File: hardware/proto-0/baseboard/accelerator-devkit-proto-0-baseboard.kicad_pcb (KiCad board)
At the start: 6 copper layers, 50 x 42 mm, 175 parts, among them J1 JTAG, J2 USB-C, J3 HDMI, J4 Qwiic I2C, J5 Pmod 1A, J6 Pmod 1B, J7 Display, J8 microSD-ST11-H, Q1 CSD13381F4, SW1 BUTTON1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

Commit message: Onigiri <3
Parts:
- LOGO2: moved to B.Cu
- LOGO3: moved to F.Cu
- moved LOGO2 0.11 mm to (6.55, 26.4), turned to 180 degrees
- moved LOGO3 0.05 mm to (6.60, 26.1), turned to 10 degrees

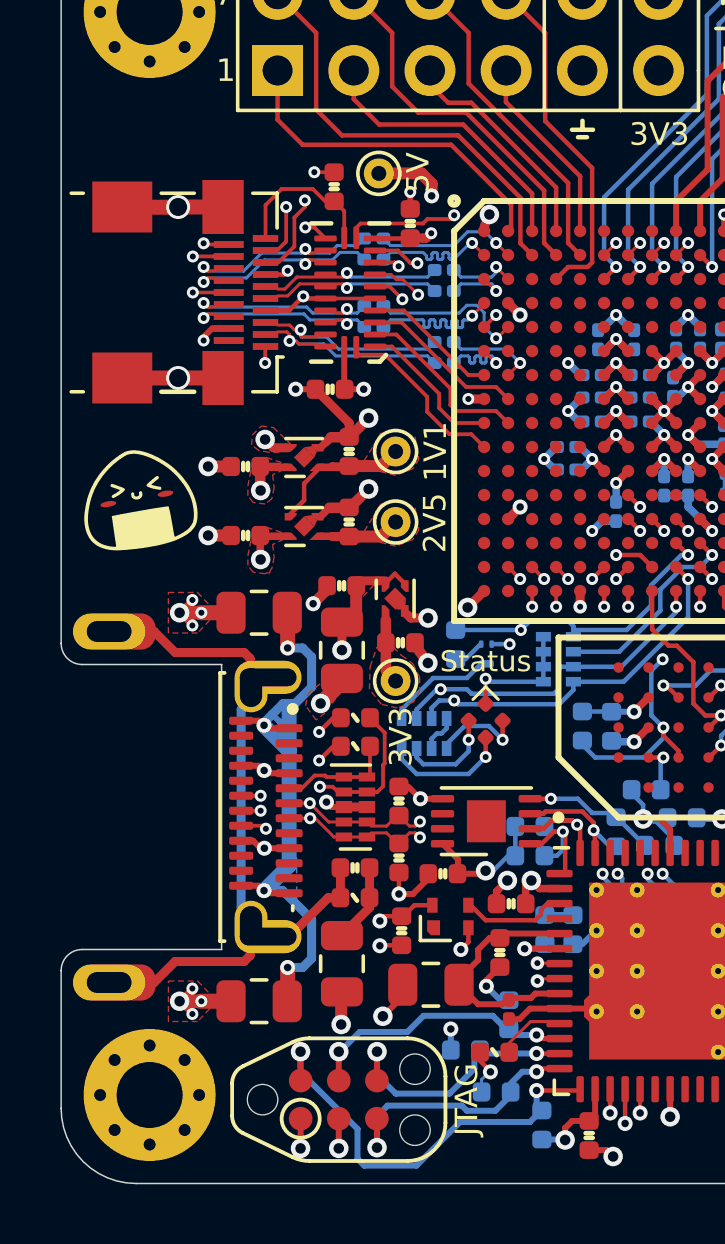
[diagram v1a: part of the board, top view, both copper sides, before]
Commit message: Switching USB connector to CUI UJ31-CH-3-MSMT-TR-67
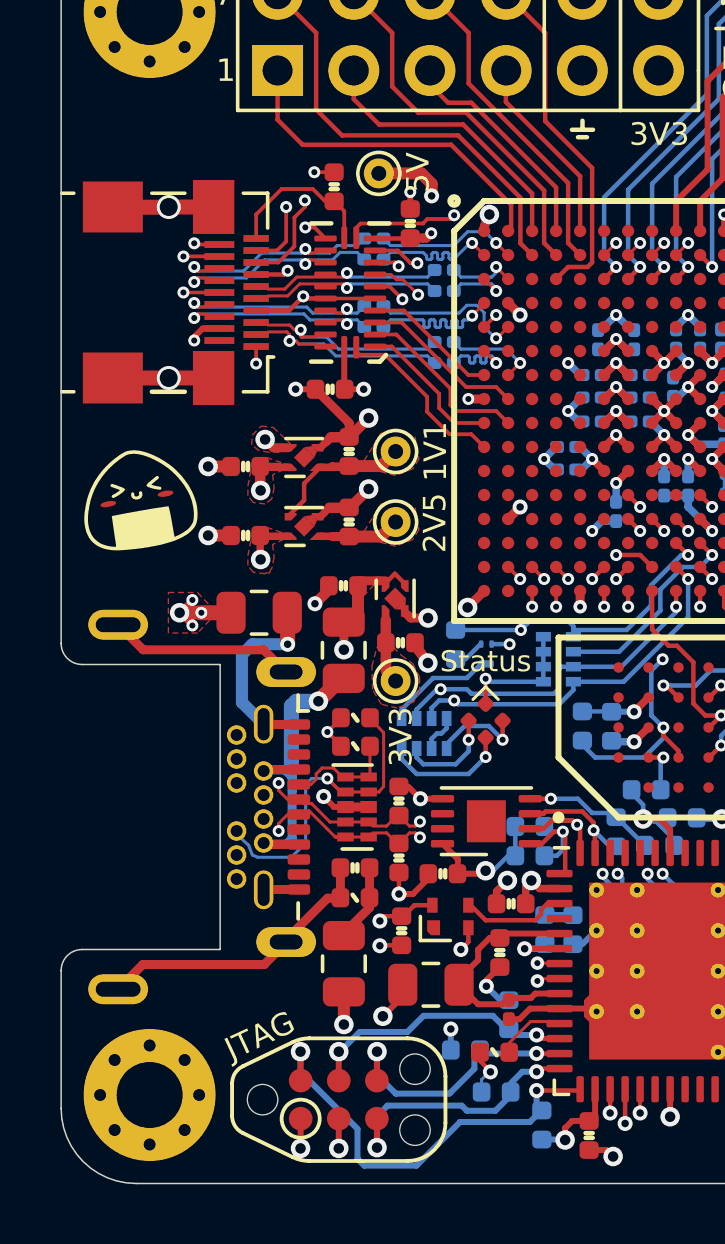
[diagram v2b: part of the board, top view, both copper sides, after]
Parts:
- removed FB5: 1K/1A, Inductor_SMD:L_0805_2012Metric
- J2: footprint Connector_USB_RD:JAE_DX07B024JJ1R1500 -> Connector_USB_RD:CUI_UJ31-CH-3-MSMT-TR-67
- moved J2 5.00 mm to (5.90, 36.5)
- moved J3 0.31 mm to (5.72, 19.3)
- moved FB4 0.07 mm to (13.4, 41.7)
- moved C1 0.06 mm to (13.4, 29.1)
- moved FB1 0.06 mm to (13.4, 31.2)
- moved U9 0.05 mm to (13.9, 36.5)
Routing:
- net /USB-I/O/USB_UNSAFE_GND: track 22.2 -> 13.9 mm, vias 4 -> 1
- net /USB-I/O/USB_SHIELD: track 21.8 -> 25.7 mm
- net GND: track 174.1 -> 170.4 mm, vias 127 -> 122
- net /USB-I/O/USB_CC2: track 9.39 -> 10.7 mm, vias 2 -> 1
- net /USB-I/O/USB_D-: track 17.5 -> 16.4 mm, vias 4 -> 3
- net /USB-I/O/USB_D+: track 17.5 -> 16.7 mm, vias 4 -> 3
- net /HDMI-IO/HDMI_CON_SCL: track 10.1 -> 10.8 mm
- net /HDMI-IO/HDMI_CON_CEC: track 11.5 -> 12.2 mm
- net /HDMI-IO/HDMI_CON_TMDS_CK-: track 6.84 -> 7.46 mm
- net /HDMI-IO/HDMI_CON_TMDS_D1-: track 6.57 -> 7.09 mm
- net /USB-I/O/USB_UNSAFE_VBUS: track 10.5 -> 10.6 mm, vias 3 -> 1
- removed copper zone on B.Cu, net /USB-I/O/USB_UNSAFE_GND
- removed copper zone on F.Cu, net /USB-I/O/USB_UNSAFE_VBUS

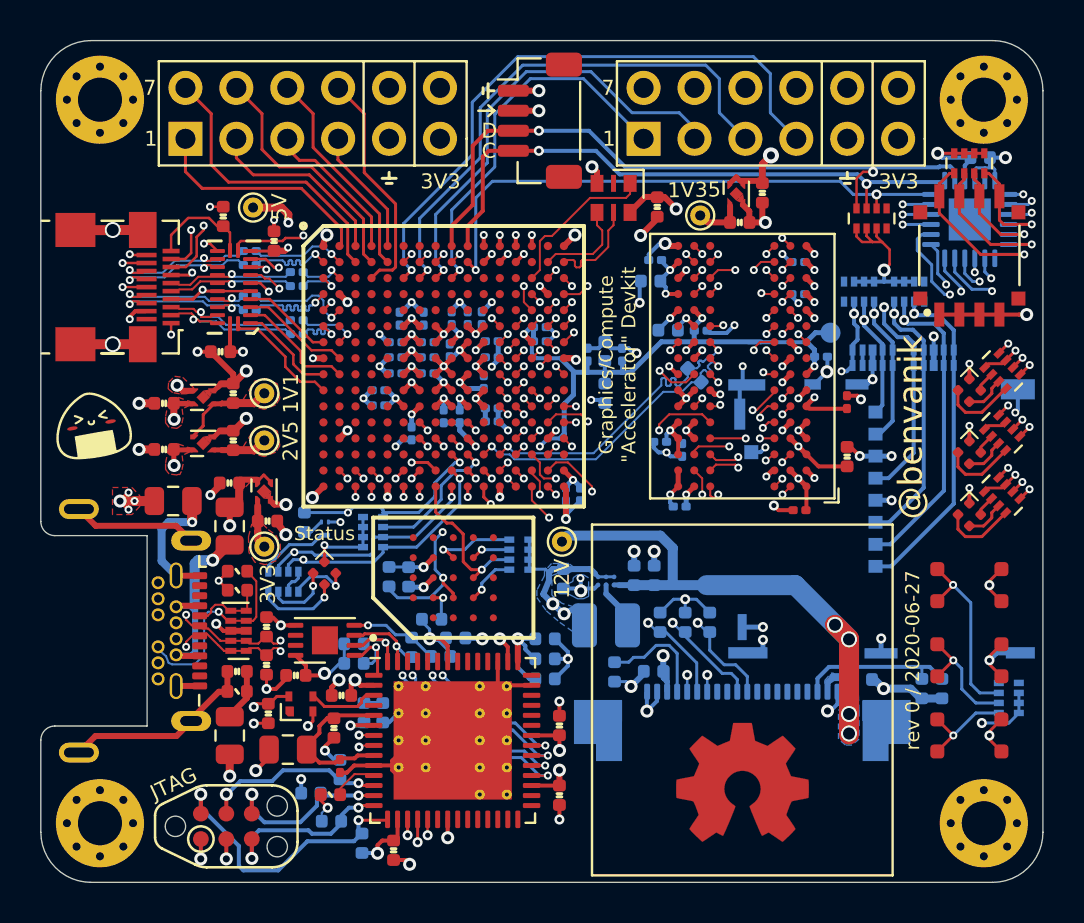
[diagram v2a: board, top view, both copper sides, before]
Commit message: Adding fiducials and marking as rev 0A
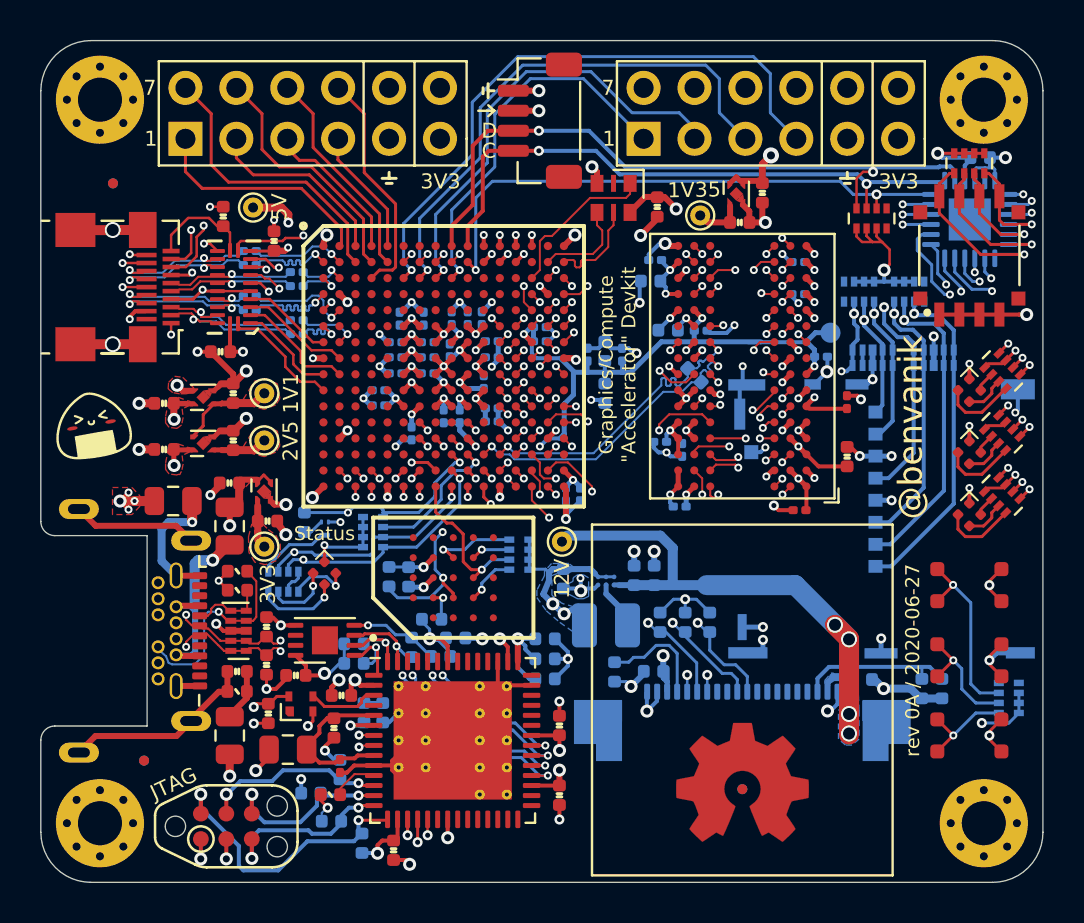
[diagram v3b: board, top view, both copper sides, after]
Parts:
- added REF**: Fiducial_0.5mm_Mask1mm, Fiducial:Fiducial_0.5mm_Mask1mm, B.Cu at (9.15, 42.9)
- added REF**: Fiducial_0.5mm_Mask1mm, Fiducial:Fiducial_0.5mm_Mask1mm, B.Cu at (7.60, 14.1)
- added REF**: Fiducial_0.5mm_Mask1mm, Fiducial:Fiducial_0.5mm_Mask1mm, B.Cu at (39.0, 44.4)
- added REF**: Fiducial_0.5mm_Mask1mm, Fiducial:Fiducial_0.5mm_Mask1mm, F.Cu at (39.0, 44.4)
- added REF**: Fiducial_0.5mm_Mask1mm, Fiducial:Fiducial_0.5mm_Mask1mm, F.Cu at (9.15, 42.9)
- added REF**: Fiducial_0.5mm_Mask1mm, Fiducial:Fiducial_0.5mm_Mask1mm, F.Cu at (7.60, 14.1)
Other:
- board text added: "rev 0A / 2020-06-27"
- board text removed: "rev 0 / 2020-06-27"
